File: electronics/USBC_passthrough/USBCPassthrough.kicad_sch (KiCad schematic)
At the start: 2 parts, among them J1 USB_C_Receptacle_USB2.0_16P, J2 USB_C_Receptacle_USB2.0_16P

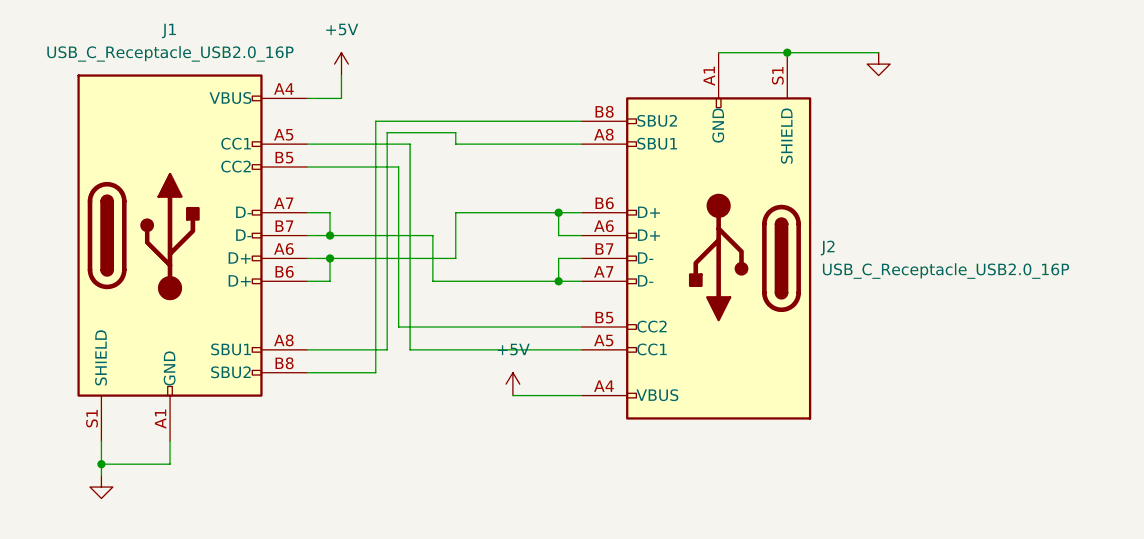
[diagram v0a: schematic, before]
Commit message: fixed passthrough circuit
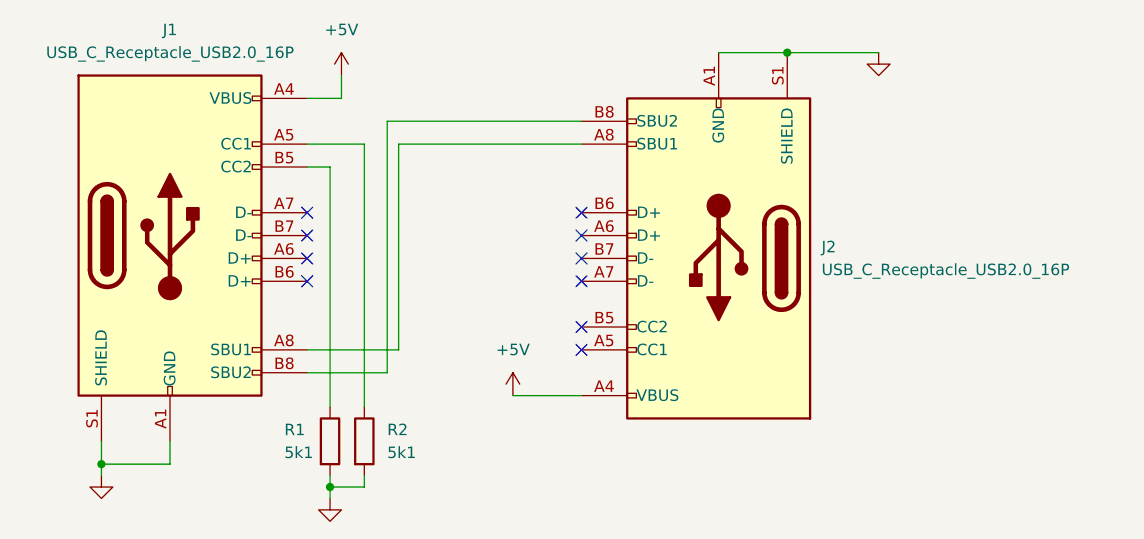
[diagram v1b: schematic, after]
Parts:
- added R1, R2: 5k1, Resistor_SMD:R_0603_1608Metric, symbol Device:R
- J1: footprint (none) -> Library:TYPE-C-SMD_USB4120-03-C
- J2: footprint (none) -> Library:USB-C-SMD_TYPEC-302-BRP16SC16
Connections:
- net GND: now also R1.2, R2.2
- net at J2.A5 (CC1): no longer J1.A5 (CC1)
- net at J2.B5 (CC2): no longer J1.B5 (CC2)
- new net: J1.B5 (CC2), R1.1
- new net: J1.A5 (CC1), R2.1
- now unconnected: J1.A6 (D+), J1.A7 (D-), J1.B6 (D+), J1.B7 (D-), J2.A6 (D+), J2.A7 (D-), J2.B6 (D+), J2.B7 (D-)
- no-connect marks 0 -> 10
